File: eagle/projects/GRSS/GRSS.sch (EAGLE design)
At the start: 32 parts, among them J1 MOL-SL-2-RA, J10 MOL-SL-2-RA, J11 M02PTH, J2 MOL-SL-2-RA, J3 MOL-SL-2-RA, J4 MOL-SL-2-RA, J5 MOL-SL-2-RA, J6 MOL-SL-2-RA, J7 MOL-SL-2-RA, J8 MOL-SL-2-RA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

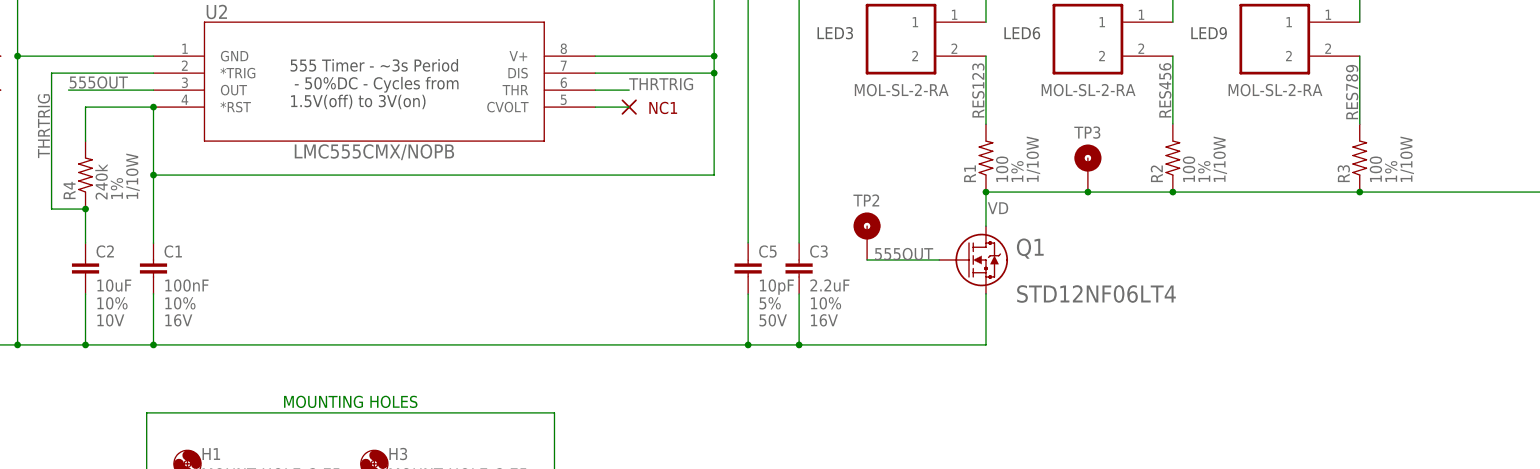
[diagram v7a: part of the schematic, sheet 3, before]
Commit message: Updated Resistors to be 0805 and added 3 0805 res to Lib
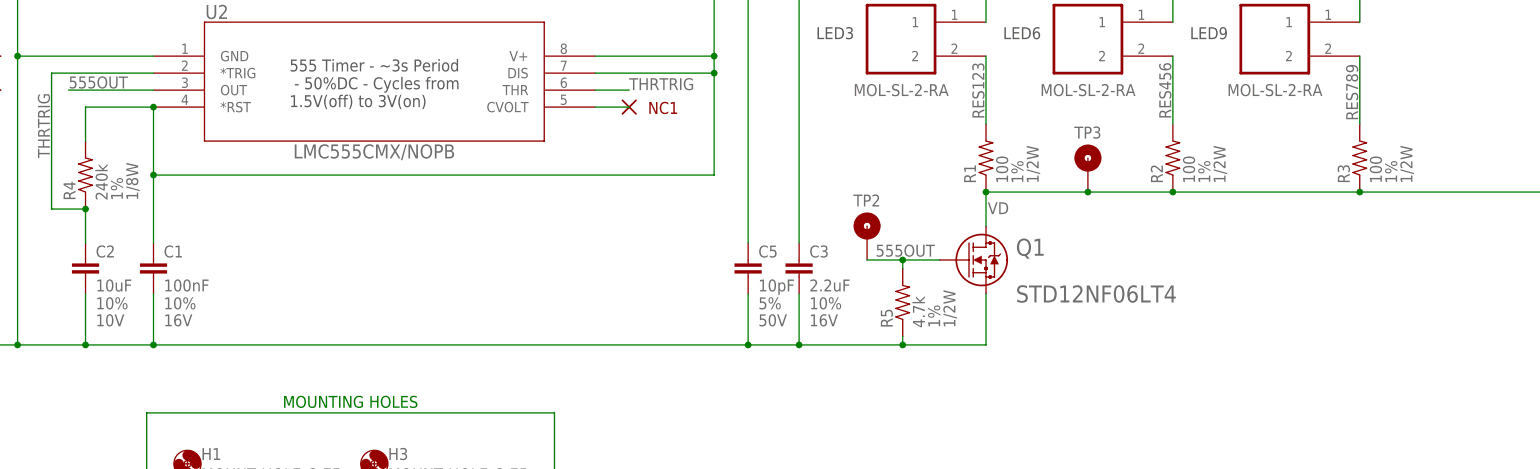
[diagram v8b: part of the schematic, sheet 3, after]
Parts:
- added R5: 4.7k, grss:RES_47R0_0805
- R1, R2, R3: device grss:RES_100R_0603 -> grss:RES_100R0_0805
- R4: device grss:RES_240R0_0603 -> grss:RES_240R0_0805
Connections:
- net 555OUT: now also R5.2
- net GND: now also R5.1
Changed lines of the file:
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@@
 <parts>
 <part name="BATT" library="grss" deviceset="BC9VPC" device="" value="9V"/>
-<part name="R1" library="grss" deviceset="RES" device="_0603" technology="_100R" value="100"/>
-<part name="R2" library="grss" deviceset="RES" device="_0603" technology="_100R" value="100"/>
-<part name="R3" library="grss" deviceset="RES" device="_0603" technology="_100R" value="100"/>
-<part name="R4" library="grss" deviceset="RES" device="_0603" technology="_240R0" value="240k"/>
+<part name="R1" library="grss" deviceset="RES" device="_0805" technology="_100R0" value="100"/>
+<part name="R2" library="grss" deviceset="RES" device="_0805" technology="_100R0" value="100"/>
+<part name="R3" library="grss" deviceset="RES" device="_0805" technology="_100R0" value="100"/>
+<part name="R4" library="grss" deviceset="RES" device="_0805" technology="_240R0" value="240k"/>
 <part name="C1" library="grss" deviceset="CAP" device="_0603" technology="_100NF0" value="100nF"/>
 <part name="C2" library="grss" deviceset="CAP" device="_0603" technology="_10UF0" value="10uF"/>
@@
 <part name="H4" library="grss" deviceset="MOUNT-HOLE" device="_2.75"/>
 <part name="U$2" library="grss" deviceset="BLOCK_DIAGRAM" device=""/>
+<part name="R5" library="grss" deviceset="RES" device="_0805" technology="_47R0" value="4.7k"/>
 </parts>
 <sheets>
@@
 <instance part="H3" gate="G$1" x="-116.84" y="73.66"/>
 <instance part="H4" gate="G$1" x="-116.84" y="66.04"/>
+<instance part="R5" gate="G$1" x="-37.846" y="97.79" rot="R90"/>
 </instances>
 <busses>
@@
 <pinref part="U2" gate="A" pin="GND"/>
 <pinref part="U3" gate="A" pin="GND"/>
-<wire x1="-53.34" y1="91.44" x2="-25.4" y2="91.44" width="0.1524" layer="91"/>
+<wire x1="-53.34" y1="91.44" x2="-37.846" y2="91.44" width="0.1524" layer="91"/>
 <junction x="-53.34" y="91.44"/>
 <pinref part="GND1" gate="1" pin="GND"/>
 <junction x="-177.8" y="91.44"/>
 <pinref part="Q1" gate="A" pin="3"/>
+<wire x1="-37.846" y1="91.44" x2="-25.4" y2="91.44" width="0.1524" layer="91"/>
 <wire x1="-25.4" y1="91.44" x2="-25.4" y2="99.06" width="0.1524" layer="91"/>
+<pinref part="R5" gate="G$1" pin="1"/>
+<wire x1="-37.846" y1="91.44" x2="-37.846" y2="92.71" width="0.1524" layer="91"/>
+<junction x="-37.846" y="91.44"/>
 </segment>
 </net>
@@
 </segment>
 <segment>
-<wire x1="-32.385" y1="104.14" x2="-43.18" y2="104.14" width="0.1524" layer="91"/>
-<label x="-42.164" y="104.14" size="1.778" layer="95"/>
+<wire x1="-32.385" y1="104.14" x2="-37.846" y2="104.14" width="0.1524" layer="91"/>
+<label x="-41.91" y="104.648" size="1.778" layer="95"/>
 <pinref part="Q1" gate="A" pin="1"/>
 <pinref part="TP2" gate="G$1" pin="TP"/>
-</segment>
-</net>
+<pinref part="R5" gate="G$1" pin="2"/>
+<wire x1="-37.846" y1="104.14" x2="-43.18" y2="104.14" width="0.1524" layer="91"/>
+<wire x1="-37.846" y1="102.87" x2="-37.846" y2="104.14" width="0.1524" layer="91"/>
+<junction x="-37.846" y="104.14"/>
+</segment>
+</net>
